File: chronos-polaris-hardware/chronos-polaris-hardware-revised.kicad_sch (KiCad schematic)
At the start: 31 parts, among them J1 Conn_01x03_Pin, J10 TSW-102-07-G-D, J2 Conn_01x03_Pin, J3 Conn_01x03_Pin, J4 Conn_01x03_Pin, J5 Conn_01x03_Pin, J6 Conn_01x04, J7 Conn_01x04, J8 Conn_01x02, J9 691417320006S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

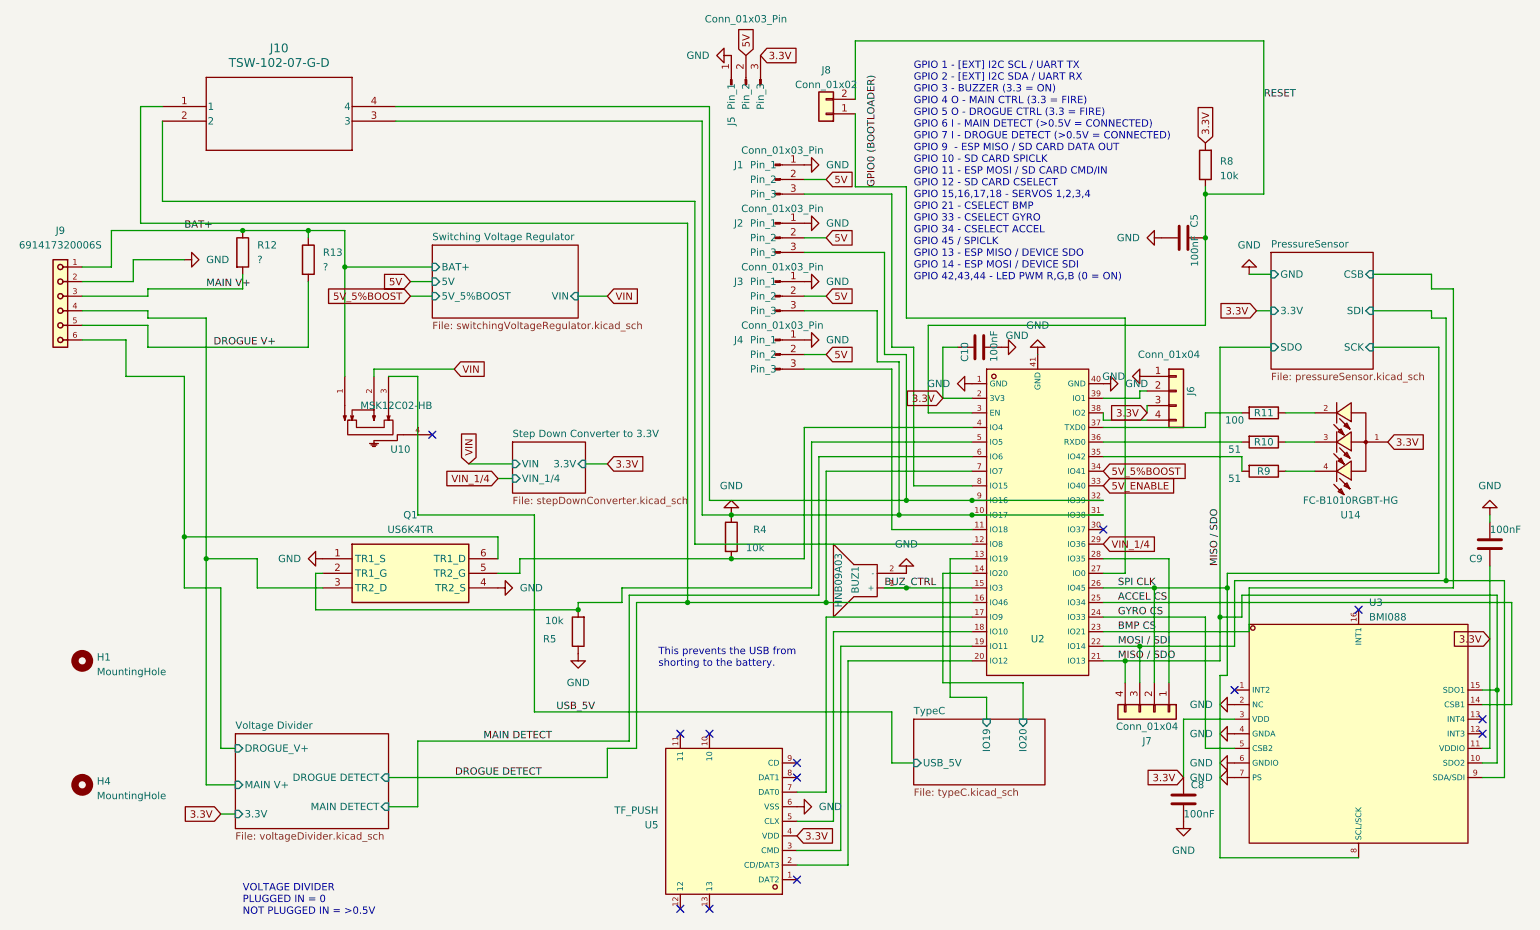
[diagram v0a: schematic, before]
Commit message: Schematic Changes as per DR1 Suggestions
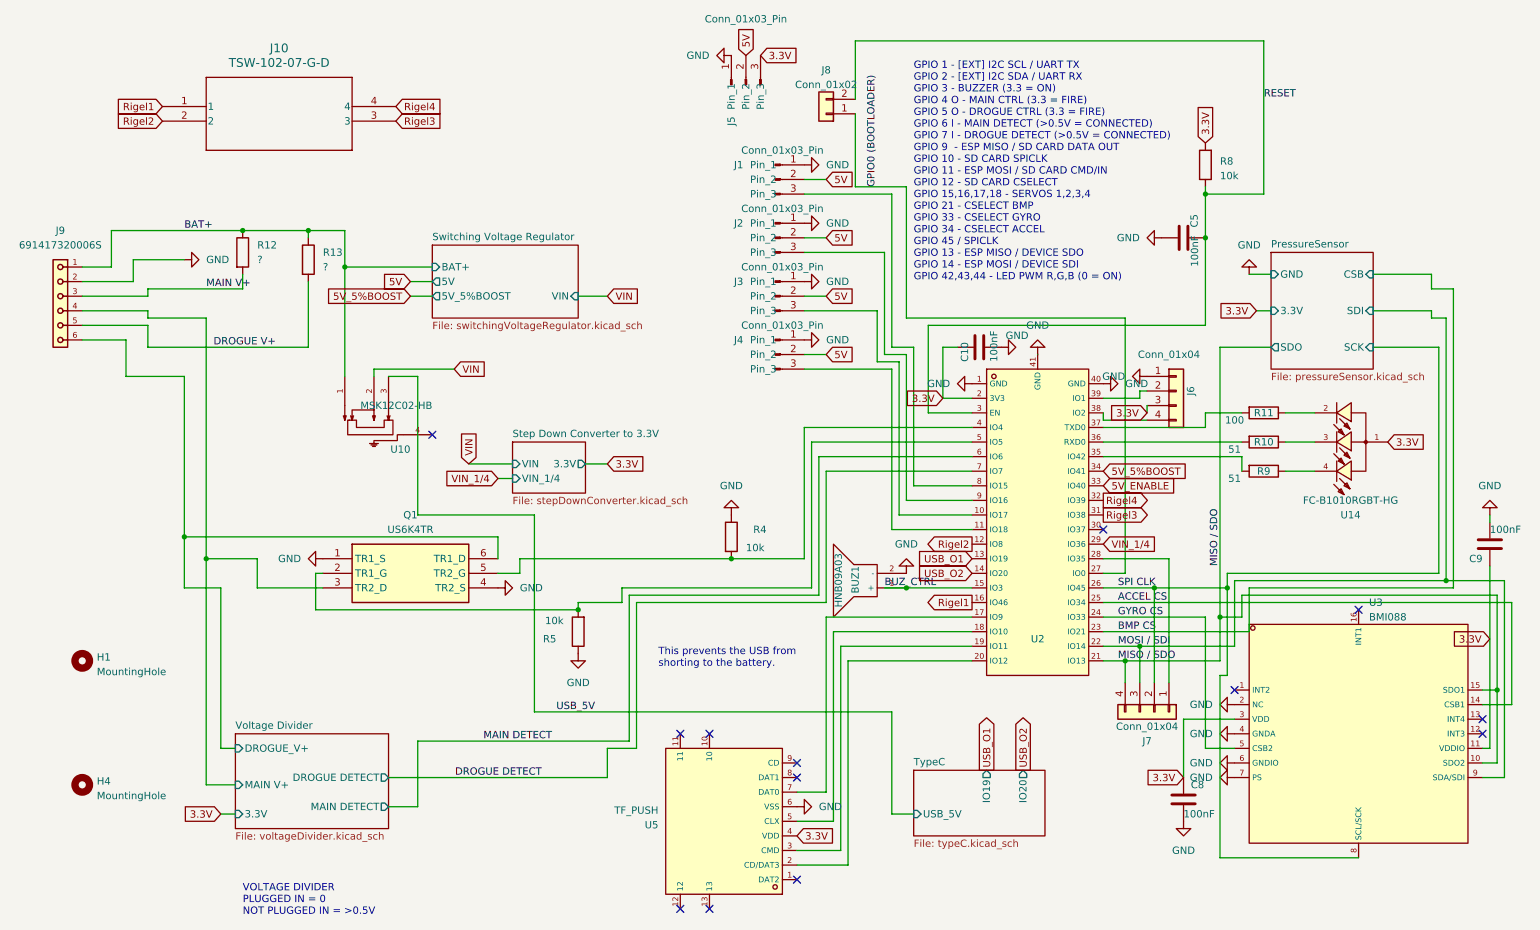
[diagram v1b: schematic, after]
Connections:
- net DROGUE DETECT: no longer J10.1, U2.16 (IO46)
- net GND: no longer J10.3, J3.3 (Pin_3), U2.10 (IO17), U2.31 (IO38)
- net Rigel2: now reaches J10.2, U2.12 (IO8)
- net at J2.3 (Pin_3), U2.9 (IO16): no longer J10.4, U2.32 (IO39)
- net TypeC/IO19 renamed USB_O1
- net TypeC/IO20 renamed USB_O2
- new net: J3.3 (Pin_3), U2.10 (IO17)
- new net Rigel1: J10.1, U2.16 (IO46)
- new net Rigel3: J10.3, U2.31 (IO38)
- new net Rigel4: J10.4, U2.32 (IO39)

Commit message: fixes. - Rishik B.
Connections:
- net 3.3V: now also J10.3
- net GND: now also J10.4
- net Rigel3: no longer names the net of U2.31 (IO38)
- net Rigel3: no longer J10.3
- net Rigel4: no longer names the net of U2.32 (IO39)
- net Rigel4: no longer J10.4
- no-connect marks 13 -> 15
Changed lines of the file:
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@@
 	)
 	(no_connect
+		(at 213.36 100.33)
+	)
+	(no_connect
 		(at 139.7 171.45)
 	)
@@
 	)
 	(no_connect
+		(at 213.36 102.87)
+	)
+	(no_connect
 		(at 213.36 105.41)
 	)
@@
 	(wire
 		(pts
+			(xy 90.17 35.56) (xy 90.17 34.29)
+		)
+		(stroke
+			(width 0)
+			(type default)
+		)
+	)
+	(wire
+		(pts
 			(xy 46.99 63.5) (xy 63.5 63.5)
 		)
@@
 	(wire
 		(pts
+			(xy 90.17 31.75) (xy 91.44 31.75)
+		)
+		(stroke
+			(width 0)
+			(type default)
+		)
+	)
+	(wire
+		(pts
 			(xy 161.29 87.63) (xy 161.29 110.49)
 		)
@@
 	(wire
 		(pts
+			(xy 92.71 35.56) (xy 90.17 35.56)
+		)
+		(stroke
+			(width 0)
+			(type default)
+		)
+	)
+	(wire
+		(pts
 			(xy 234.95 115.57) (xy 234.95 113.03)
 		)
@@
 		)
 	)
-	(global_label "Rigel3"
-		(shape output)
-		(at 213.36 102.87 0)
-		(fields_autoplaced yes)
-		(effects
-			(font
-				(size 1.27 1.27)
-			)
-			(justify left)
-		)
-		(property "Intersheetrefs" "${INTERSHEET_REFS}"
-			(at 222.3323 102.87 0)
-			(effects
-				(font
-					(size 1.27 1.27)
-				)
-				(justify left)
-				(hide yes)
-			)
-		)
-	)
 	(global_label "3.3V"
 		(shape input)
@@
 		)
 	)
-	(global_label "Rigel4"
-		(shape input)
-		(at 90.17 31.75 0)
-		(fields_autoplaced yes)
-		(effects
-			(font
-				(size 1.27 1.27)
-			)
-			(justify left)
-		)
-		(property "Intersheetrefs" "${INTERSHEET_REFS}"
-			(at 99.1423 31.75 0)
-			(effects
-				(font
-					(size 1.27 1.27)
-				)
-				(justify left)
-				(hide yes)
-			)
-		)
-	)
 	(global_label "3.3V"
 		(shape input)
@@
 		)
 	)
-	(global_label "Rigel3"
-		(shape input)
-		(at 90.17 34.29 0)
-		(fields_autoplaced yes)
-		(effects
-			(font
-				(size 1.27 1.27)
-			)
-			(justify left)
-		)
-		(property "Intersheetrefs" "${INTERSHEET_REFS}"
-			(at 99.1423 34.29 0)
-			(effects
-				(font
-					(size 1.27 1.27)
-				)
-				(justify left)
-				(hide yes)
-			)
-		)
-	)
 	(global_label "Rigel1"
 		(shape output)
@@
 		)
 	)
-	(global_label "Rigel4"
-		(shape output)
-		(at 213.36 100.33 0)
+	(global_label "3.3V"
+		(shape input)
+		(at 92.71 35.56 0)
 		(fields_autoplaced yes)
 		(effects
@@
 		)
 		(property "Intersheetrefs" "${INTERSHEET_REFS}"
-			(at 222.3323 100.33 0)
+			(at 99.8076 35.56 0)
 			(effects
 				(font
@@
 		(lib_name "GND_1")
 		(lib_id "power:GND")
+		(at 91.44 31.75 90)
+		(unit 1)
+		(exclude_from_sim no)
+		(in_bom yes)
+		(on_board yes)
+		(dnp no)
+		(fields_autoplaced yes)
+		(property "Reference" "#PWR057"
+			(at 97.79 31.75 0)
+			(effects
+				(font
+					(size 1.27 1.27)
+				)
+				(hide yes)
+			)
+		)
+		(property "Value" "GND"
+			(at 95.25 31.7499 90)
+			(effects
+				(font
+					(size 1.27 1.27)
+				)
+				(justify right)
+			)
+		)
+		(property "Footprint" ""
+			(at 91.44 31.75 0)
+			(effects
+				(font
+					(size 1.27 1.27)
+				)
+				(hide yes)
+			)
+		)
+		(property "Datasheet" ""
+			(at 91.44 31.75 0)
+			(effects
+				(font
+					(size 1.27 1.27)
+				)
+				(hide yes)
+			)
+		)
+		(property "Description" "Power symbol creates a global label with name \"GND\" , ground"
+			(at 91.44 31.75 0)
+			(effects
+				(font
+					(size 1.27 1.27)
+				)
+				(hide yes)
+			)
+		)
+		(pin "1"
+		)
+		(instances
+			(project "chronos-polaris-hardware-revised"
+				(path "/503f01d5-a0c6-4ade-b485-97c3c2e1d6c5"
+					(reference "#PWR057")
+					(unit 1)
+				)
+			)
+		)
+	)
+	(symbol
+		(lib_name "GND_1")
+		(lib_id "power:GND")
 		(at 236.22 140.97 270)
 		(unit 1)
@@
 			)
 		)
-		(pin "SDO" output
+		(pin "SDO" bidirectional
 			(at 242.57 73.66 180)
 			(effects
@@
 			)
 		)
-		(pin "SDI" input
+		(pin "SDI" bidirectional
 			(at 260.35 67.31 0)
 			(effects
